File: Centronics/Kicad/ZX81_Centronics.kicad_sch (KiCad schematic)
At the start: 16 parts, among them J1 CENTRONICS, Q1 BC558, SW1 SW_Push, U1 74LS27, U2 74LS32, U3 74LS30, U4 8255

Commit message: Work in progress
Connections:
- net GND: now also BUS1.4B (GND), BUS1.5B (GND)
- net VCC: now also BUS1.1B (5V)
- net ~{RD}: now also BUS1.16A (~{RD})
- net ~{WR}: now also BUS1.17A (~{WR})
- net D7: now reaches BUS1.1A (D7)
- no-connect marks 0 -> 1
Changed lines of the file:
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@@
   (junction (at 259.08 132.08) (diameter 0) (color 0 0 0 0)
   )
+  (junction (at 22.86 140.97) (diameter 0) (color 0 0 0 0)
+  )
   (junction (at 100.33 157.48) (diameter 0) (color 0 0 0 0)
   )
@@
   (junction (at 76.2 132.08) (diameter 0) (color 0 0 0 0)
   )
+  (no_connect (at 22.86 133.35))
   (wire (pts (xy 22.86 76.2) (xy 72.39 76.2))
     (stroke (width 0) (type default))
@@
     (stroke (width 0) (type default))
   )
+  (wire (pts (xy 15.24 140.97) (xy 22.86 140.97))
+    (stroke (width 0) (type default))
+  )
   (wire (pts (xy 22.86 48.26) (xy 49.53 48.26))
     (stroke (width 0) (type default))
@@
     (stroke (width 0) (type default))
   )
+  (wire (pts (xy 22.86 138.43) (xy 22.86 140.97))
+    (stroke (width 0) (type default))
+  )
   (wire (pts (xy 222.25 78.74) (xy 218.44 78.74))
     (stroke (width 0) (type default))
@@
     (effects (font (size 1.27 1.27)) (justify left bottom))
   )
+  (label "~{RD}" (at 53.34 168.91 0) (fields_autoplaced)
+    (effects (font (size 1.27 1.27)) (justify left bottom))
+  )
   (label "11B" (at 234.95 93.98 0) (fields_autoplaced)
     (effects (font (size 1.27 1.27)) (justify left bottom))
@@
     (effects (font (size 1.27 1.27)) (justify right bottom))
   )
+  (label "D7" (at 53.34 130.81 0) (fields_autoplaced)
+    (effects (font (size 1.27 1.27)) (justify left bottom))
+  )
   (label "11A" (at 222.25 93.98 180) (fields_autoplaced)
     (effects (font (size 1.27 1.27)) (justify right bottom))
   )
   (label "7B" (at 207.01 109.22 0) (fields_autoplaced)
+    (effects (font (size 1.27 1.27)) (justify left bottom))
+  )
+  (label "~{WR}" (at 53.34 171.45 0) (fields_autoplaced)
     (effects (font (size 1.27 1.27)) (justify left bottom))
   )
@@
         (path "/2b9b9cb5-15d9-4155-82b8-4ddd7fb75fd7"
           (reference "SW1") (unit 1)
+        )
+      )
+    )
+  )
+  (symbol (lib_id "power:GND") (at 15.24 140.97 0) (unit 1)
+    (in_bom yes) (on_board yes) (dnp no) (fields_autoplaced)
+    (property "Reference" "#PWR011" (at 15.24 147.32 0)
+      (effects (font (size 1.27 1.27)) hide)
+    )
+    (property "Value" "GND" (at 15.24 146.05 0)
+      (effects (font (size 1.27 1.27)))
+    )
+    (property "Footprint" "" (at 15.24 140.97 0)
+      (effects (font (size 1.27 1.27)) hide)
+    )
+    (property "Datasheet" "" (at 15.24 140.97 0)
+      (effects (font (size 1.27 1.27)) hide)
+    )
+    (pin "1")
+    (instances
+      (project "ZX81_Centronics"
+        (path "/2b9b9cb5-15d9-4155-82b8-4ddd7fb75fd7"
+          (reference "#PWR011") (unit 1)
         )
       )
@@
         )
       )
+    )
+  )
+  (symbol (lib_id "power:VCC") (at 22.86 130.81 0) (unit 1)
+    (in_bom yes) (on_board yes) (dnp no) (fields_autoplaced)
+    (property "Reference" "#PWR012" (at 22.86 134.62 0)
+      (effects (font (size 1.27 1.27)) hide)
+    )
+    (property "Value" "VCC" (at 22.86 125.73 0)
+      (effects (font (size 1.27 1.27)))
+    )
+    (property "Footprint" "" (at 22.86 130.81 0)
+      (effects (font (size 1.27 1.27)) hide)
+    )
+    (property "Datasheet" "" (at 22.86 130.81 0)
+      (effects (font (size 1.27 1.27)) hide)
+    )
+    (pin "1")
+    (instances
+      (project "ZX81_Centronics"
+        (path "/2b9b9cb5-15d9-4155-82b8-4ddd7fb75fd7"
+          (reference "#PWR012") (unit 1)
+        )
+      )

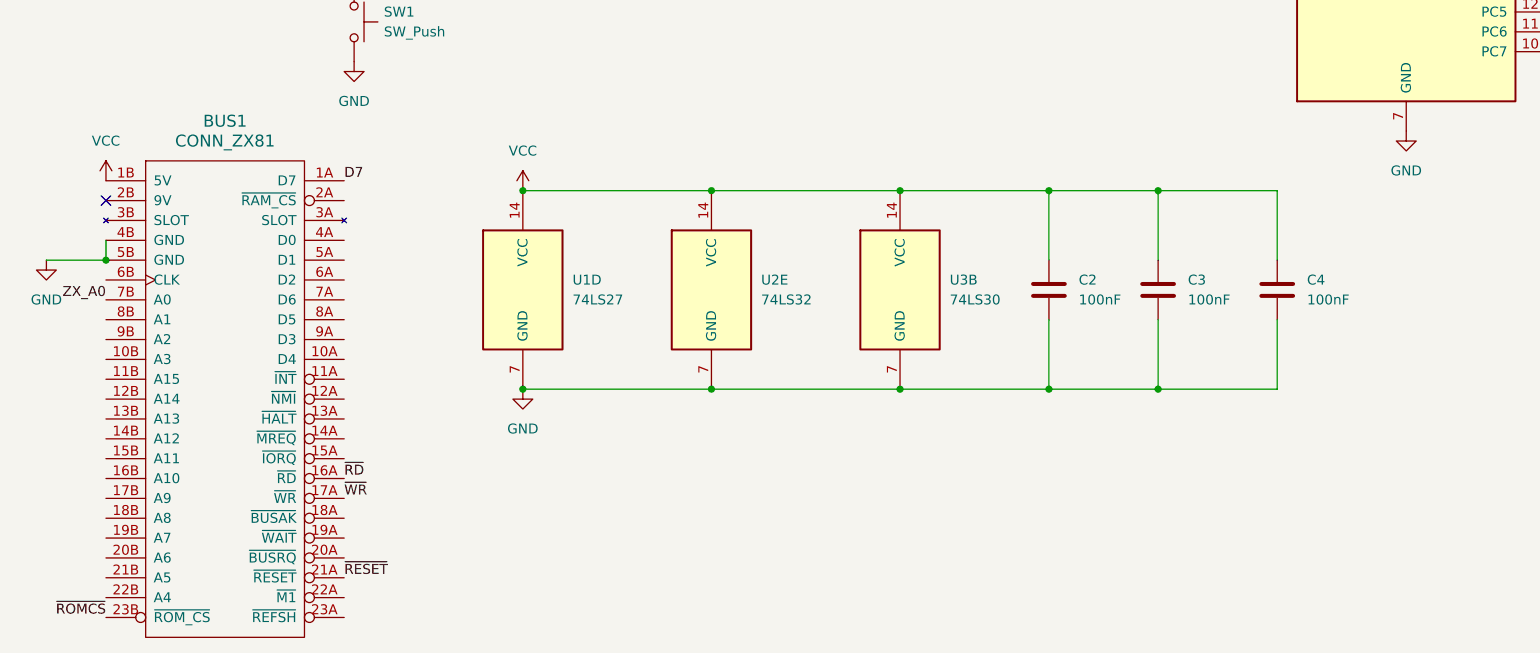
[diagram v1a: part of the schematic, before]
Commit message: Basic schematic finished
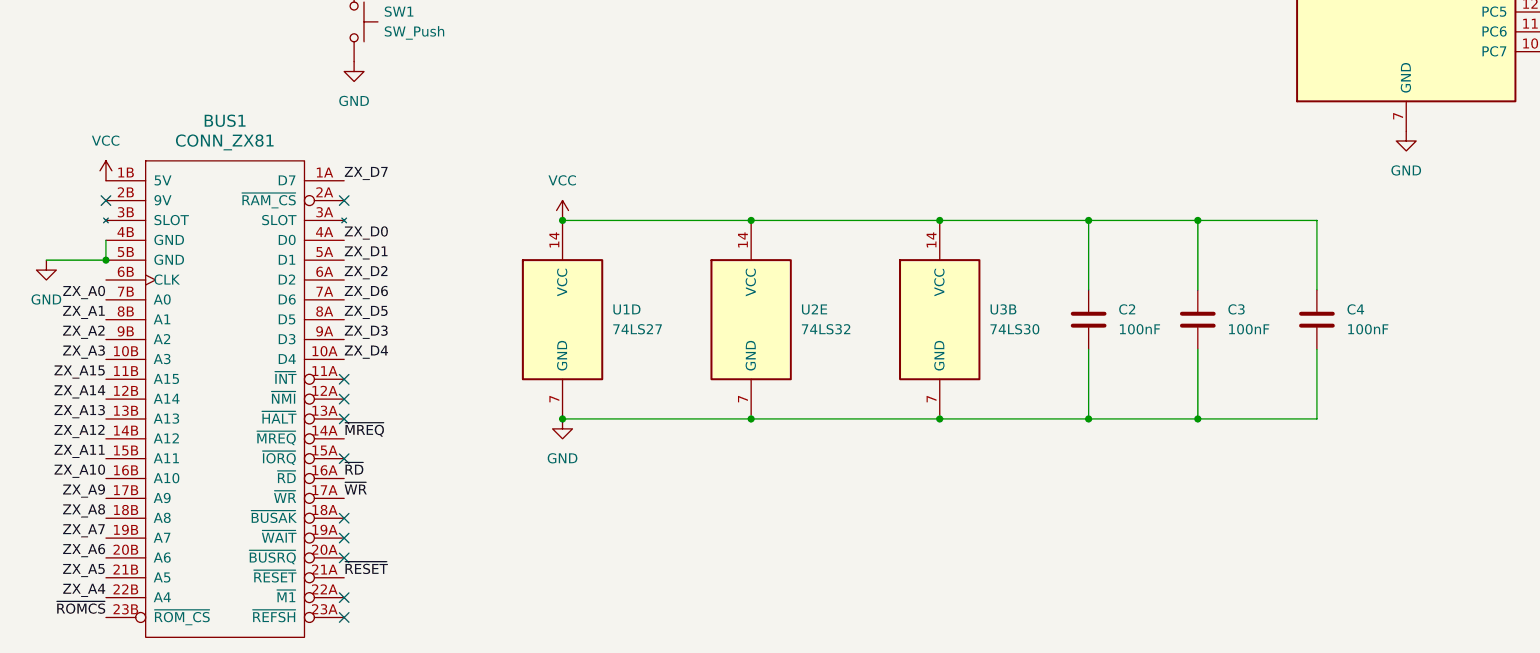
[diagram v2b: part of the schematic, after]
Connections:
- net D7 is gone; now on net ZX_D7: BUS1.1A (D7)
- net ZX_A1: now also BUS1.8B (A1)
- net ZX_A10: now also BUS1.16B (A10)
- net ZX_A11: now also BUS1.15B (A11)
- net ZX_A12: now also BUS1.14B (A12)
- net ZX_A13: now also BUS1.13B (A13)
- net ZX_A14: now also BUS1.12B (A14)
- net ZX_A15: now also BUS1.11B (A15)
- net ZX_A2: now also BUS1.9B (A2)
- net ZX_A3: now also BUS1.10B (A3)
- net ZX_A4: now also BUS1.22B (A4)
- net ZX_A5: now also BUS1.21B (A5)
- net ZX_A6: now also BUS1.20B (A6)
- net ZX_A7: now also BUS1.19B (A7)
- net ZX_A8: now also BUS1.18B (A8)
- net ZX_A9: now also BUS1.17B (A9)
- net ZX_D0: now also BUS1.4A (D0)
- net ZX_D1: now also BUS1.5A (D1)
- net ZX_D2: now also BUS1.6A (D2)
- net ZX_D3: now also BUS1.9A (D3)
- net ZX_D4: now also BUS1.10A (D4)
- net ZX_D5: now also BUS1.8A (D5)
- net ZX_D6: now also BUS1.7A (D6)
- net ~{MREQ}: now also BUS1.14A (~{MREQ})
- no-connect marks 1 -> 11
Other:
- moved on the sheet: C2, C3, C4, U1D, U2E, U3B

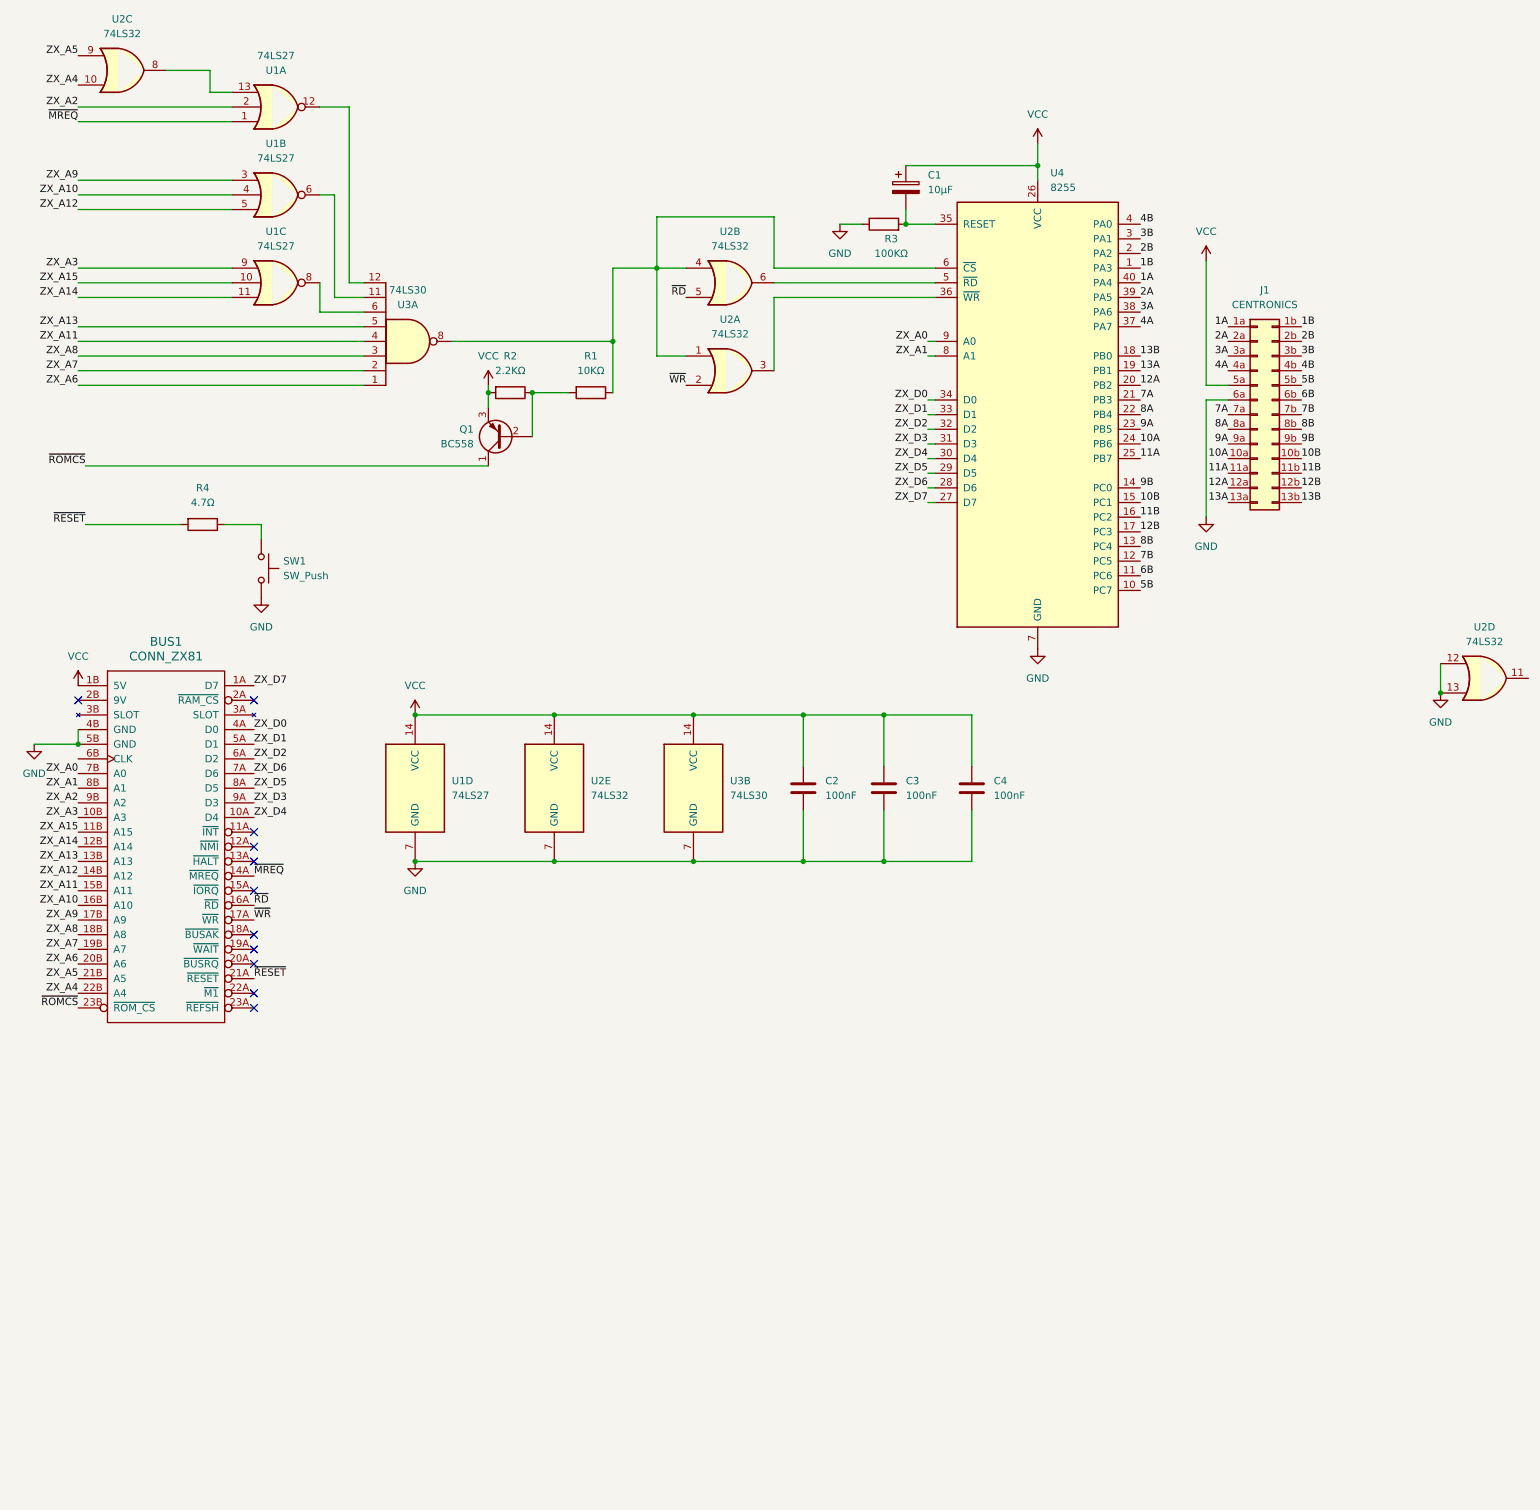
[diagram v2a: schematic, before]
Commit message: Added English auto-translation
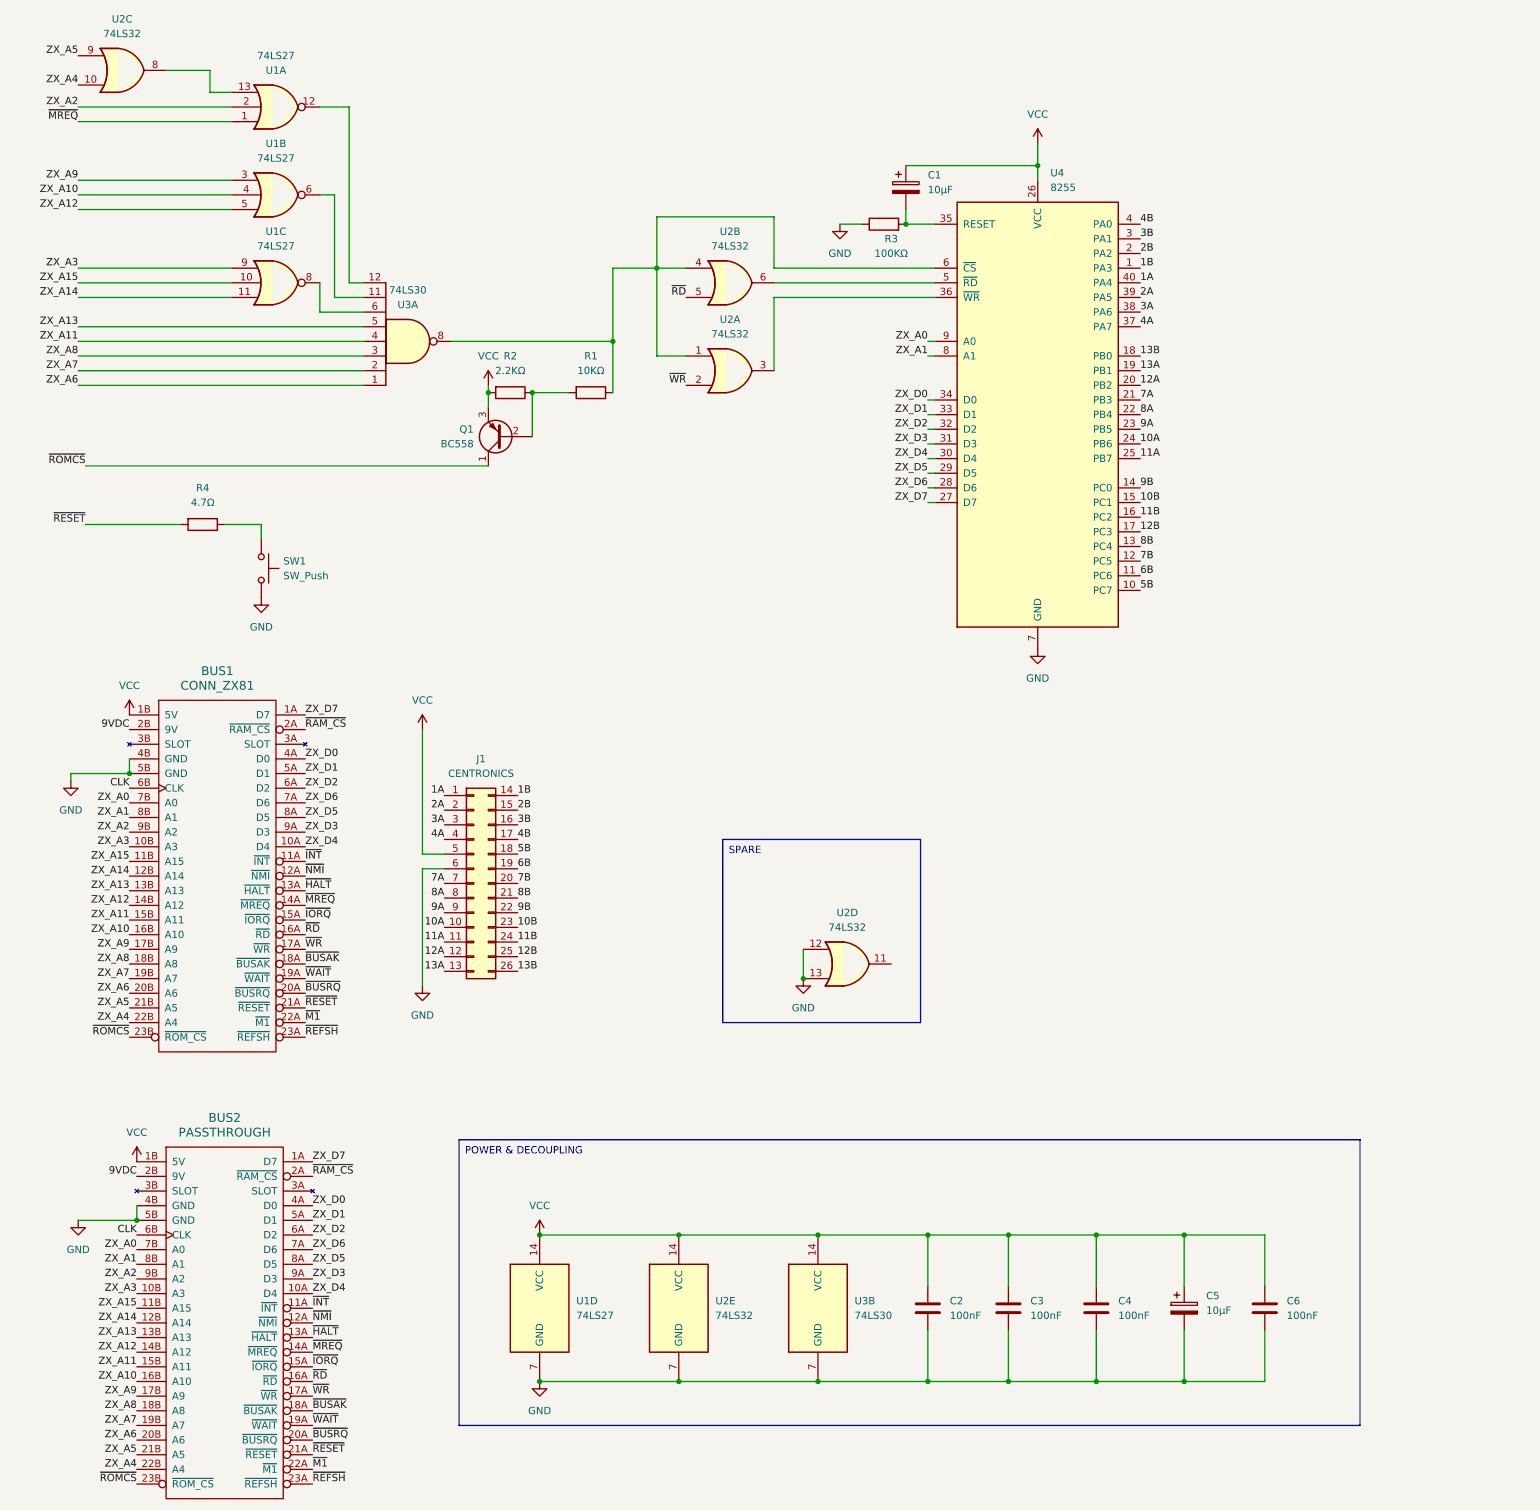
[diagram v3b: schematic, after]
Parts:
- added BUS2: PASSTHROUGH, CluelessEngineer:ZX81_EDGE, symbol my_components:CONN_ZX81
- added C5: 10µF, Capacitor_THT:CP_Radial_D5.0mm_P2.50mm, symbol Device:C_Polarized
- added C6: 100nF, symbol Device:C
- BUS1: footprint (none) -> CluelessEngineer:ZX81_EDGE
- C1: footprint (none) -> Capacitor_THT:CP_Radial_D5.0mm_P2.50mm
- C2, C3, C4: footprint (none) -> Capacitor_THT:C_Disc_D4.3mm_W1.9mm_P5.00mm
- J1: footprint (none) -> Connector_PinHeader_2.54mm:PinHeader_2x13_P2.54mm_Vertical; symbol Connector_Generic:Conn_02x13_Row_Letter_Last -> Connector_Generic:Conn_02x13_Top_Bottom
- R1, R2, R3, R4: footprint (none) -> Resistor_THT:R_Axial_DIN0207_L6.3mm_D2.5mm_P7.62mm_Horizontal
- SW1: footprint (none) -> Button_Switch_THT:KSA_Tactile_SPST
- U1, U2, U3: footprint (none) -> Package_DIP:DIP-14_W7.62mm
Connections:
- net 10A: now also J1.10 (Pin_10); no longer J1.10a (Pin_10a)
- net 10B: now also J1.23 (Pin_23); no longer J1.10b (Pin_10b)
- net 11A: now also J1.11 (Pin_11); no longer J1.11a (Pin_11a)
- net 11B: now also J1.24 (Pin_24); no longer J1.11b (Pin_11b)
- net 12A: now also J1.12 (Pin_12); no longer J1.12a (Pin_12a)
- net 12B: now also J1.25 (Pin_25); no longer J1.12b (Pin_12b)
- net 13A: now also J1.13 (Pin_13); no longer J1.13a (Pin_13a)
- net 13B: now also J1.26 (Pin_26); no longer J1.13b (Pin_13b)
- net 1A: now also J1.1 (Pin_1); no longer J1.1a (Pin_1a)
- net 1B: now also J1.14 (Pin_14); no longer J1.1b (Pin_1b)
- net 2A: now also J1.2 (Pin_2); no longer J1.2a (Pin_2a)
- net 2B: now also J1.15 (Pin_15); no longer J1.2b (Pin_2b)
- net 3A: now also J1.3 (Pin_3); no longer J1.3a (Pin_3a)
- net 3B: now also J1.16 (Pin_16); no longer J1.3b (Pin_3b)
- net 4A: now also J1.4 (Pin_4); no longer J1.4a (Pin_4a)
- net 4B: now also J1.17 (Pin_17); no longer J1.4b (Pin_4b)
- net 5B: now also J1.18 (Pin_18); no longer J1.5b (Pin_5b)
- net 6B: now also J1.19 (Pin_19); no longer J1.6b (Pin_6b)
- net 7A: now also J1.7 (Pin_7); no longer J1.7a (Pin_7a)
- net 7B: now also J1.20 (Pin_20); no longer J1.7b (Pin_7b)
- net 8A: now also J1.8 (Pin_8); no longer J1.8a (Pin_8a)
- net 8B: now also J1.21 (Pin_21); no longer J1.8b (Pin_8b)
- net 9A: now also J1.9 (Pin_9); no longer J1.9a (Pin_9a)
- net 9B: now also J1.22 (Pin_22); no longer J1.9b (Pin_9b)
- net GND: now also J1.6 (Pin_6), BUS2.4B (GND), BUS2.5B (GND), C5.2, C6.2; no longer J1.6a (Pin_6a)
- net VCC: now also J1.5 (Pin_5), BUS2.1B (5V), C5.1, C6.1; no longer J1.5a (Pin_5a)
- net ZX_A0: now also BUS2.7B (A0)
- net ZX_A1: now also BUS2.8B (A1)
- net ZX_A10: now also BUS2.16B (A10)
- net ZX_A11: now also BUS2.15B (A11)
- net ZX_A12: now also BUS2.14B (A12)
- net ZX_A13: now also BUS2.13B (A13)
- net ZX_A14: now also BUS2.12B (A14)
- net ZX_A15: now also BUS2.11B (A15)
- net ZX_A2: now also BUS2.9B (A2)
- net ZX_A3: now also BUS2.10B (A3)
- net ZX_A4: now also BUS2.22B (A4)
- net ZX_A5: now also BUS2.21B (A5)
- net ZX_A6: now also BUS2.20B (A6)
- net ZX_A7: now also BUS2.19B (A7)
- net ZX_A8: now also BUS2.18B (A8)
- net ZX_A9: now also BUS2.17B (A9)
- net ZX_D0: now also BUS2.4A (D0)
- net ZX_D1: now also BUS2.5A (D1)
- net ZX_D2: now also BUS2.6A (D2)
- net ZX_D3: now also BUS2.9A (D3)
- net ZX_D4: now also BUS2.10A (D4)
- net ZX_D5: now also BUS2.8A (D5)
- net ZX_D6: now also BUS2.7A (D6)
- net ZX_D7: now also BUS2.1A (D7)
- net ~{MREQ}: now also BUS2.14A (~{MREQ})
- net ~{RD}: now also BUS2.16A (~{RD})
- net ~{RESET}: now also BUS2.21A (~{RESET})
- net ~{ROMCS}: now also BUS2.23B (~{ROM_CS})
- net ~{WR}: now also BUS2.17A (~{WR})
- net ~{INT}: now reaches BUS1.11A (~{INT})
- net ~{INT}: now also BUS2.11A (~{INT})
- net ~{NMI}: now reaches BUS1.12A (~{NMI})
- net ~{NMI}: now also BUS2.12A (~{NMI})
- net ~{HALT}: now reaches BUS1.13A (~{HALT})
- net ~{HALT}: now also BUS2.13A (~{HALT})
- net ~{IORQ}: now reaches BUS1.15A (~{IORQ})
- net ~{IORQ}: now also BUS2.15A (~{IORQ})
- net ~{BUSAK}: now reaches BUS1.18A (~{BUSAK})
- net ~{BUSAK}: now also BUS2.18A (~{BUSAK})
- net ~{WAIT}: now reaches BUS1.19A (~{WAIT})
- net ~{WAIT}: now also BUS2.19A (~{WAIT})
- net ~{BUSRQ}: now reaches BUS1.20A (~{BUSRQ})
- net ~{BUSRQ}: now also BUS2.20A (~{BUSRQ})
- net ~{M1}: now reaches BUS1.22A (~{M1})
- net ~{M1}: now also BUS2.22A (~{M1})
- net ~{REFSH}: now reaches BUS1.23A (~{REFSH})
- net ~{REFSH}: now also BUS2.23A (~{REFSH})
- net ~{RAM_CS}: now reaches BUS1.2A (~{RAM_CS})
- net ~{RAM_CS}: now also BUS2.2A (~{RAM_CS})
- net 9VDC: now reaches BUS1.2B (9V)
- net 9VDC: now also BUS2.2B (9V)
- net CLK: now reaches BUS1.6B (CLK)
- net CLK: now also BUS2.6B (CLK)
- no-connect marks 11 -> 0
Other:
- moved on the sheet: BUS1, C2, C3, C4, J1, U1D, U2D, U2E, U3B
